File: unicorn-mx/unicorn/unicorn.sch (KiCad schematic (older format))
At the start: 157 parts, among them J1 Conn_01x06, J2 USB_C, J3 Conn_01x06, J4 Conn_01x04, J5 Conn_01x04, J6 Conn_01x04, K1 KEYSW, K10 KEYSW, K11 KEYSW, K12 KEYSW, K13 KEYSW, K14 KEYSW, K15 KEYSW, K16 KEYSW, K17 KEYSW, K18 KEYSW, K19 KEYSW, K2 KEYSW, K20 KEYSW, K21 KEYSW, K22 KEYSW, K23 KEYSW, K24 KEYSW, K25 KEYSW, K26 KEYSW, K27 KEYSW, K28 KEYSW, K29 KEYSW, K3 KEYSW, K30 KEYSW, K31 KEYSW, K32 KEYSW, K33 KEYSW, K34 KEYSW, K35 KEYSW, K36 KEYSW, K37 KEYSW, K38 KEYSW, K39 KEYSW, K4 KEYSW, K40 KEYSW, K41 KEYSW, K42 KEYSW, K43 KEYSW, K44 KEYSW, K5 KEYSW, K6 KEYSW, K7 KEYSW, K8 KEYSW, K9 KEYSW, Q1 MMBT3904, SW1 SW_Push, SW2 Rotary_Encoder_Switch, SW3 Rotary_Encoder_Switch, U1 XC6206PxxxMR, U2 STM32F411CCUx, U4 SRV05-4, Y1 25M Hz, Y2 32.768KHz

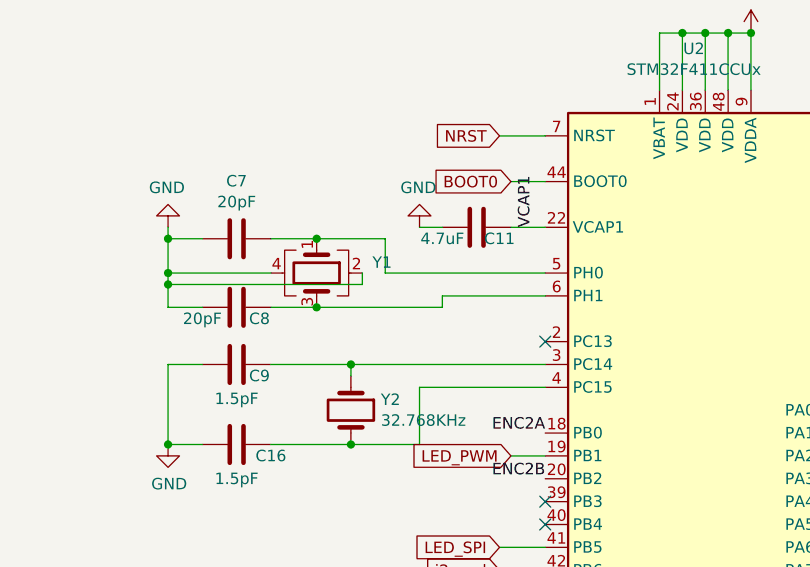
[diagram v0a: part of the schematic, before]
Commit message: Add back rotation for jlcpcb positions, as most footproints still needs rotation.
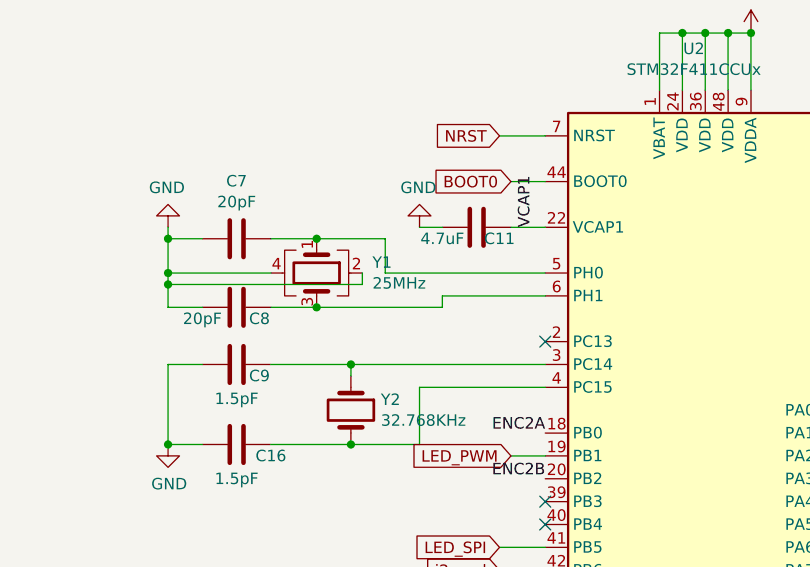
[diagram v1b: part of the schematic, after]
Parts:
- Y1: value 25M Hz -> 25MHz
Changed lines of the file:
@@
 P 7150 6900
 F 0 "Y1" V 7104 7144 50  0000 L CNN
-F 1 "25MHz" V 7195 7144 50  0000 L CNN
+F 1 "25MHz" V 7195 7144 50  0000 L CNN
 F 2 "Crystal:Crystal_SMD_3225-4Pin_3.2x2.5mm" H 7150 6900 50  0001 C CNN
 F 3 "" H 7150 6900 50  0001 C CNN
